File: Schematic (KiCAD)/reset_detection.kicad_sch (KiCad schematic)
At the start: 57 parts, among them J69 INVERT, P29 INVERT, X15 INVERT

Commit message: - Started work on the pulse channels.  - Solved at least 2 of the red traces in the SVG.  - Finally realized that "Unknown 4to1" cells are actually just ordinary And-Or-Invert "AOI22" cells.
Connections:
- net at OSC4. (X): now also OSC3. (X); no longer OSC5. (X)
- net at OSC3. (X): now also OSC2. (X); no longer OSC4. (X)
- net at D41. (X): now also D42. (X); no longer D40. (X)
- net at BM23. (X): now also BM24. (/Q); no longer BM22(a). (/Q)
- net at BM24. (/Q): no longer BM23. (X)
- net at RAX3. (/Q6): now also RAX2. (X); no longer RAX1. (X)
- net at RAX4. (X): now also RAX2. (X); no longer RAX3. (/Q6)
- net at RAX7. (X): now also RAX6. (X); no longer RAX3. (/Q6)
- net at RAX5. (X): now also RAX14. (X), RAX9. (X); no longer RAX6. (X)
- net at RAX13. (X), RAX15. (X): now also RAX16. (X)
- new net: BM24. (/Q), BM25. (X), BM26. (X)
- new net: BM22(b). (/Q), BM22(c). (X)
- new net: OSC4. (X), OSC5. (X)
- new net: D40. (X), D41. (X)
- new net: BM22(a). (/Q), BM23. (X)
- new net: BM22(b). (/Q), BM23. (X)
- new net: OSC1. (X), OSC3. (X)
- new net: RAX1. (X), RAX3. (/Q6)
- new net: BM18. (X), BM19. (X), BM20. (X)
- new net: BM13,14,15,16,17. (Q3), BM19. (X) (x3)
- new net: RAX3. (/Q6), RAX4. (X)
- new net: RAX3. (/Q6), RAX7. (X)
- new net: B101. (X), B102. (X)
- new net: RAX5. (X), RAX6. (X)
- new net: RAX6. (X), RAX7. (X), RAX8. (X)
- new net: RAX10. (X), RAX13. (X), RAX9. (X)
- new net: RAX13. (X), RAX15. (X)
- new net: RAX12. (X), RAX13. (X)
- new net: BM13,14,15,16,17. (Q3), BM18. (X)
- now unconnected: BM24. (/Q)

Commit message: - Pulse DAC logic is now complete.  - The 4-bit adders are verified correct using Excel.    - This revealed 1 tracing error and also 3 XNOR gates that are actually XOR in this case.  - Now including a PDF version of the schematic.
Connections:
- net at OSC4. (X): now also OSC3. (X); no longer OSC5. (X)
- net at OSC3. (X): now also OSC2. (X); no longer OSC4. (X)
- net at D41. (X): now also D42. (X); no longer D40. (X)
- net at BM23. (X): now also BM24. (/Q); no longer BM22(a). (/Q)
- net at BM24. (/Q): no longer BM23. (X)
- net at RAX3. (/Q6): now also RAX2. (X); no longer RAX1. (X)
- net at RAX4. (X): now also RAX2. (X); no longer RAX3. (/Q6)
- net at RAX7. (X): now also RAX6. (X); no longer RAX3. (/Q6)
- net at RAX5. (X): now also RAX14. (X), RAX9. (X); no longer RAX6. (X)
- net at RAX13. (X), RAX15. (X): now also RAX16. (X)
- new net: BM24. (/Q), BM25. (X), BM26. (X)
- new net: BM22(b). (/Q), BM22(c). (X)
- new net: OSC4. (X), OSC5. (X)
- new net: D40. (X), D41. (X)
- new net: BM22(a). (/Q), BM23. (X)
- new net: BM22(b). (/Q), BM23. (X)
- new net: OSC1. (X), OSC3. (X)
- new net: RAX1. (X), RAX3. (/Q6)
- new net: BM18. (X), BM19. (X), BM20. (X)
- new net: BM13,14,15,16,17. (Q3), BM19. (X) (x3)
- new net: RAX3. (/Q6), RAX4. (X)
- new net: RAX3. (/Q6), RAX7. (X)
- new net: B101. (X), B102. (X)
- new net: RAX5. (X), RAX6. (X)
- new net: RAX6. (X), RAX7. (X), RAX8. (X)
- new net: RAX10. (X), RAX13. (X), RAX9. (X)
- new net: RAX13. (X), RAX15. (X)
- new net: RAX12. (X), RAX13. (X)
- new net: BM13,14,15,16,17. (Q3), BM18. (X)
- now unconnected: BM24. (/Q)

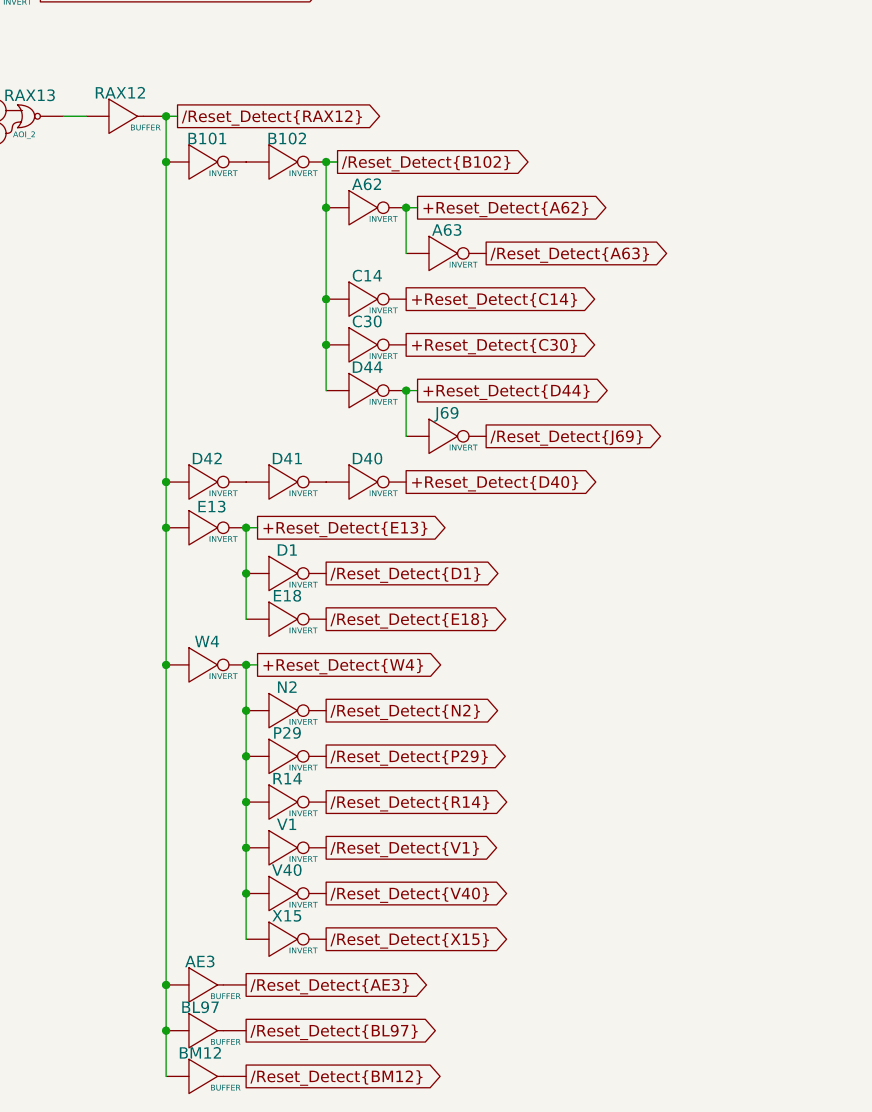
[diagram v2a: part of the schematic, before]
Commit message: - All cells in the left and center areas have now been added into the schematics.  - Changed naming of the PDF files; I was accidentally writing over furrtek's original with my new PDF.
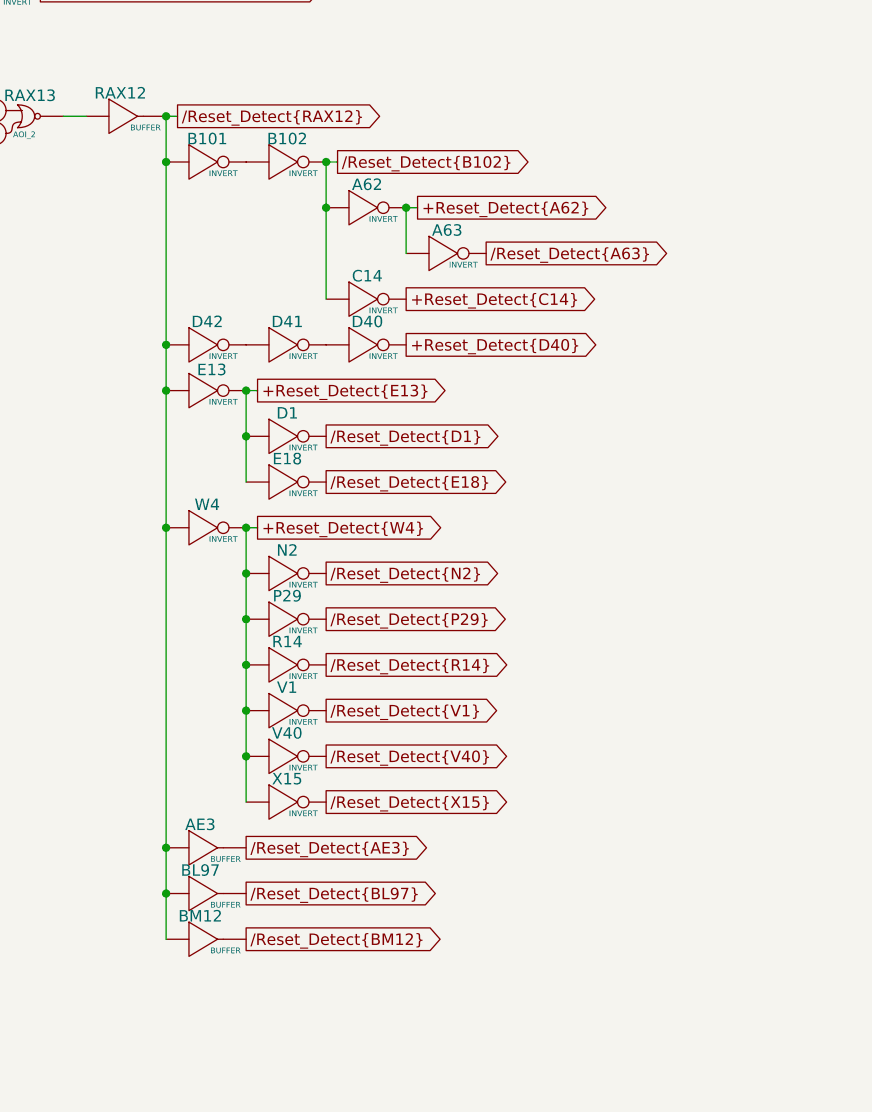
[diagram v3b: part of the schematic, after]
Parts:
- removed C30, D44, J69: INVERT, symbol MMC5:INVERT
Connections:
- net at OSC4. (X): now also OSC3. (X); no longer OSC5. (X)
- net at OSC3. (X): now also OSC2. (X); no longer OSC4. (X)
- net at D41. (X): now also D42. (X); no longer D40. (X)
- net at BM23. (X): now also BM24. (/Q); no longer BM22(a). (/Q)
- net at BM24. (/Q): no longer BM23. (X)
- net at RAX3. (/Q6): now also RAX2. (X); no longer RAX1. (X)
- net at RAX4. (X): now also RAX2. (X); no longer RAX3. (/Q6)
- net at RAX7. (X): now also RAX6. (X); no longer RAX3. (/Q6)
- net at RAX5. (X): now also RAX14. (X), RAX9. (X); no longer RAX6. (X)
- net at RAX13. (X), RAX15. (X): now also RAX16. (X)
- new net: BM24. (/Q), BM25. (X), BM26. (X)
- new net: BM22(b). (/Q), BM22(c). (X)
- new net: OSC4. (X), OSC5. (X)
- new net: D40. (X), D41. (X)
- new net: BM22(a). (/Q), BM23. (X)
- new net: BM22(b). (/Q), BM23. (X)
- new net: OSC1. (X), OSC3. (X)
- new net: RAX1. (X), RAX3. (/Q6)
- new net: BM18. (X), BM19. (X), BM20. (X)
- new net: BM13,14,15,16,17. (Q3), BM19. (X) (x3)
- new net: RAX3. (/Q6), RAX4. (X)
- new net: RAX3. (/Q6), RAX7. (X)
- new net: B101. (X), B102. (X)
- new net: RAX5. (X), RAX6. (X)
- new net: RAX6. (X), RAX7. (X), RAX8. (X)
- new net: RAX10. (X), RAX13. (X), RAX9. (X)
- new net: RAX13. (X), RAX15. (X)
- new net: RAX12. (X), RAX13. (X)
- new net: BM13,14,15,16,17. (Q3), BM18. (X)
- now unconnected: BM24. (/Q)
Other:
- moved on the sheet: AE3, BL97, BM12, D1, D40, D41, D42, E13, E18, N2, P29, R14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
